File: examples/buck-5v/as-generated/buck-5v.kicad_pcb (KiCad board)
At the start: 2 copper layers, 126 x 56 mm, 11 parts, among them J1 12V IN, J2 5V OUT, U1 LM2596S-5

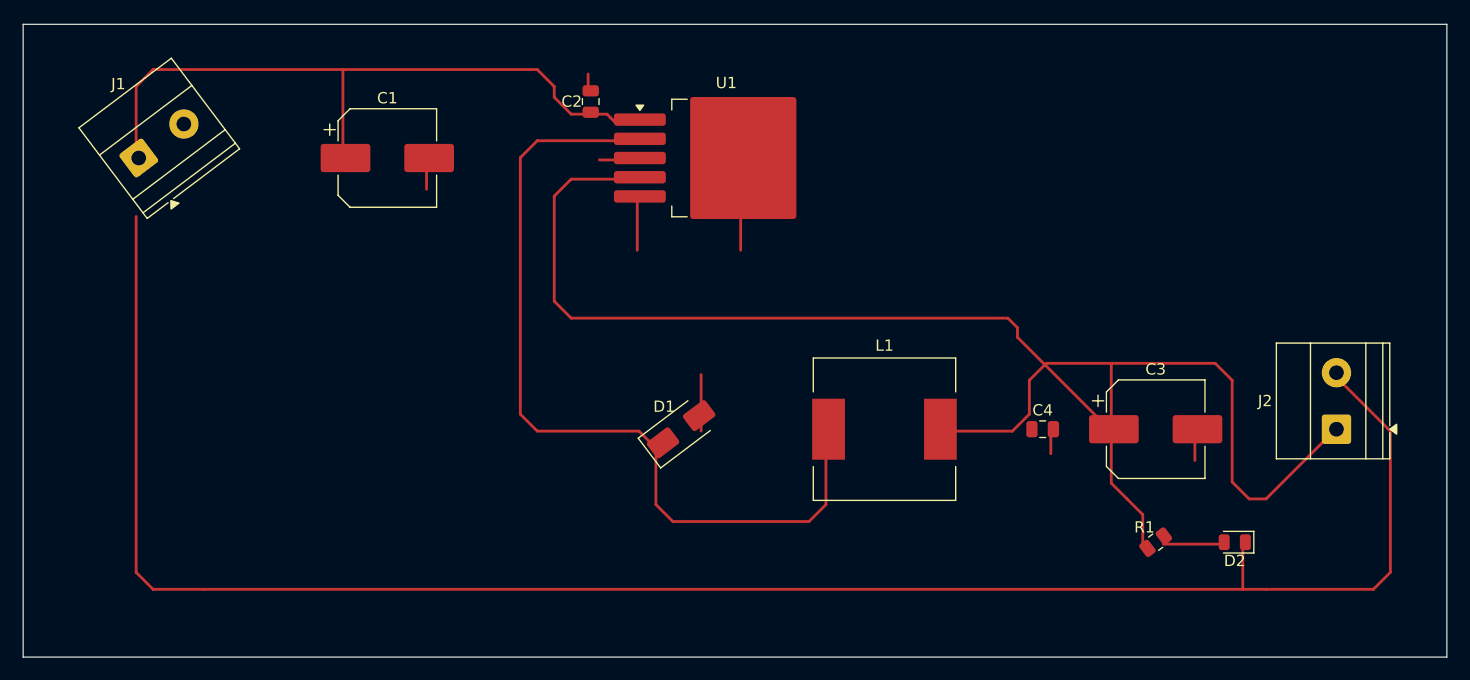
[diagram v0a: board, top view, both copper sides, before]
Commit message: Learn the drawing from the boards people drew
The brief for this round: relying on the autorouter and the numbers alone is
not enough - organise what pictorial correctness looks like from ordinary
circuits and open designs, and improve the drawing itself. So it starts in
KiCad's own demo corpus, measured and looked at, and ends with the habits
pushed into the generator.

tools/board_signature.py (new) reduces "looks autorouted" to five numbers.
Hand-routed two-layer boards cluster tightly: 10-47% of copper on the second
face, median segments 1.8-3.5 mm, 9-25 corners per decimetre, 91-98% of them
45s, 0.3-16 vias per decimetre. Rendering interf_u beside our boards says the
same thing in one glance: a layer has a direction, a bus travels as a bundle,
a person covers an offset with the long straight and one diagonal.

Three habits, now in the generator:

* Router.route(follow=...): cells beside a sibling net's path are discounted,
  so a bus (nets sharing a name prefix - I2S_*, SPI_*) travels as parallel
  lanes in one corridor. The discount is a fraction of a step, so it never
  buys a detour.
* _doglegged: every wiggly stretch is redrawn as the human stroke - the
  straight along the dominant direction plus one 45 - when the dogleg is
  clear, recursing into halves where a crossing blocks the whole. The op-amp
  board's median segment rose from 0.75 mm and its corner rate fell from
  38/dm; the FPGA board landed at 1.54 mm and 17.8/dm, inside the human band.
* Purposeful stitching: the 6 mm via carpet is gone. A ring at the rim, vias
  beside every back-layer crossing (where the plane is actually cut), and a
  coarse 12 mm mesh so no pour orphans. Vias/dm: buck 41 -> 18, carrier
  28 -> 13, all five inside the corpus band, pour_fragmented still silent.

Three failures the round produced and what they taught:

* pinned(): reshaping may not move copper off any point inside an own-net
  pad - the centre alone was not enough, a routed run touches off-centre and
  the ove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
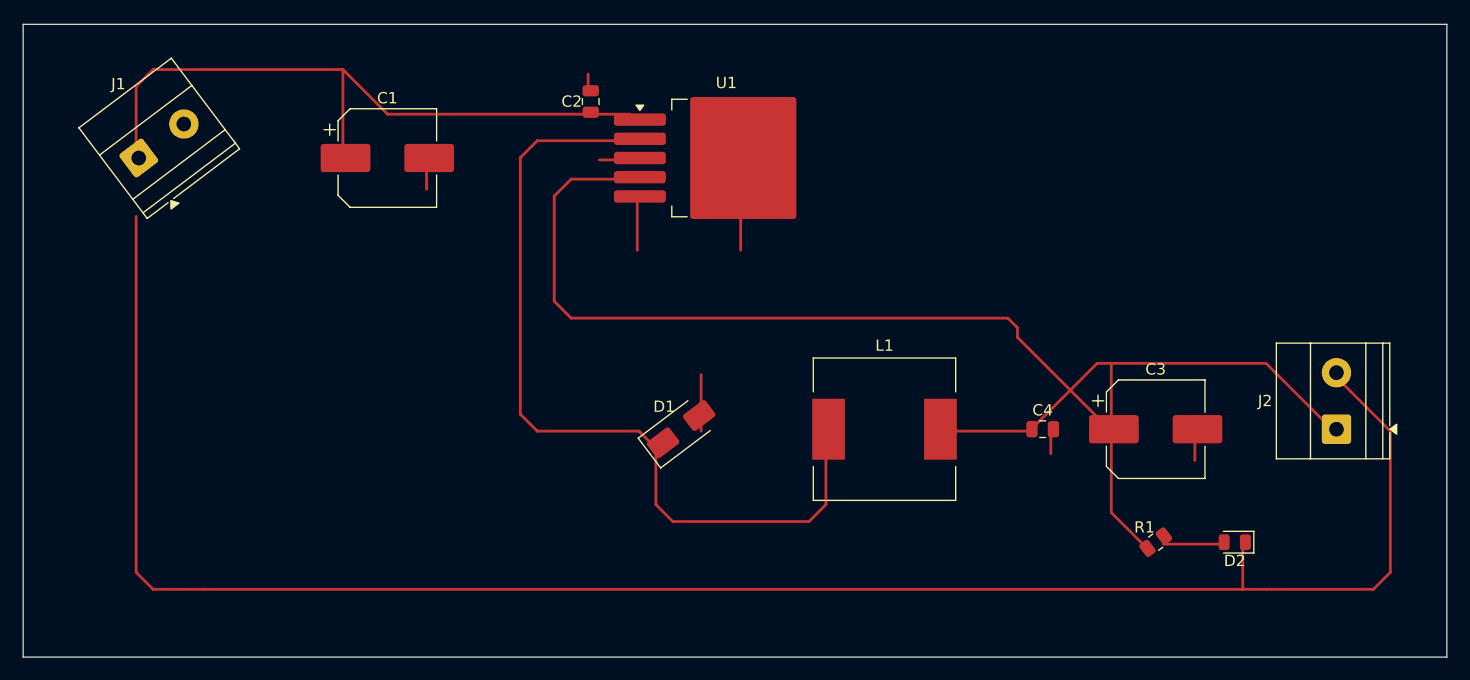
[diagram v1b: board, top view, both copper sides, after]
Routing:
- net /+5V: track 141.0 -> 129.0 mm
- net /+12V: track 61.9 -> 61.4 mm
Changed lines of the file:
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@@
 	(segment (start 111.5 64.0) (end 128.3 64.0) (width 0.25) (layer "F.Cu") (net 2))
 	(segment (start 128.3 64.0) (end 128.3 72.0) (width 0.25) (layer "F.Cu") (net 2))
-	(segment (start 128.3 64.0) (end 145.5 64.0) (width 0.25) (layer "F.Cu") (net 2))
-	(segment (start 145.5 64.0) (end 147.0 65.5) (width 0.25) (layer "F.Cu") (net 2))
-	(segment (start 147.0 65.5) (end 147.0 66.45) (width 0.25) (layer "F.Cu") (net 2))
-	(segment (start 147.0 66.45) (end 148.5 67.95) (width 0.25) (layer "F.Cu") (net 2))
-	(segment (start 148.5 67.95) (end 150.0 67.95) (width 0.25) (layer "F.Cu") (net 2))
-	(segment (start 150.0 67.95) (end 151.675 67.95) (width 0.25) (layer "F.Cu") (net 2))
-	(segment (start 151.675 67.95) (end 152.0 68.275) (width 0.25) (layer "F.Cu") (net 2))
-	(segment (start 152.0 68.275) (end 152.325 68.6) (width 0.25) (layer "F.Cu") (net 2))
-	(segment (start 152.325 68.6) (end 154.35 68.6) (width 0.25) (layer "F.Cu") (net 2))
+	(segment (start 128.3 64.0) (end 132.25 67.95) (width 0.25) (layer "F.Cu") (net 2))
+	(segment (start 132.25 67.95) (end 150.0 67.95) (width 0.25) (layer "F.Cu") (net 2))
+	(segment (start 150.0 67.95) (end 153.7 67.95) (width 0.25) (layer "F.Cu") (net 2))
+	(segment (start 153.7 67.95) (end 154.35 68.6) (width 0.25) (layer "F.Cu") (net 2))
 	(segment (start 154.35 70.3) (end 145.5 70.3) (width 0.25) (layer "F.Cu") (net 5))
 	(segment (start 145.5 70.3) (end 144.0 71.8) (width 0.25) (layer "F.Cu") (net 5))
@@
 	(segment (start 188.0 86.85) (end 188.0 87.7) (width 0.25) (layer "F.Cu") (net 3))
 	(segment (start 188.0 87.7) (end 196.3 96.0) (width 0.25) (layer "F.Cu") (net 3))
-	(segment (start 180.95 96.0) (end 187.55 96.0) (width 0.25) (layer "F.Cu") (net 3))
-	(segment (start 187.55 96.0) (end 189.05 94.5) (width 0.25) (layer "F.Cu") (net 3))
-	(segment (start 189.05 94.5) (end 189.05 91.5) (width 0.25) (layer "F.Cu") (net 3))
-	(segment (start 189.05 91.5) (end 190.55 90.0) (width 0.25) (layer "F.Cu") (net 3))
-	(segment (start 190.55 90.0) (end 196.3 90.0) (width 0.25) (layer "F.Cu") (net 3))
+	(segment (start 180.95 96.0) (end 189.05 96.0) (width 0.25) (layer "F.Cu") (net 3))
+	(segment (start 189.05 96.0) (end 195.05 90.0) (width 0.25) (layer "F.Cu") (net 3))
+	(segment (start 195.05 90.0) (end 196.3 90.0) (width 0.25) (layer "F.Cu") (net 3))
 	(segment (start 196.3 90.0) (end 196.3 96.0) (width 0.25) (layer "F.Cu") (net 3))
-	(segment (start 196.3 90.0) (end 205.5 90.0) (width 0.25) (layer "F.Cu") (net 3))
-	(segment (start 205.5 90.0) (end 207.0 91.5) (width 0.25) (layer "F.Cu") (net 3))
-	(segment (start 207.0 91.5) (end 207.0 100.5) (width 0.25) (layer "F.Cu") (net 3))
-	(segment (start 207.0 100.5) (end 208.5 102.0) (width 0.25) (layer "F.Cu") (net 3))
-	(segment (start 208.5 102.0) (end 210.0 102.0) (width 0.25) (layer "F.Cu") (net 3))
-	(segment (start 210.0 102.0) (end 216.0 96.0) (width 0.25) (layer "F.Cu") (net 3))
-	(segment (start 196.3 96.0) (end 196.3 100.606) (width 0.25) (layer "F.Cu") (net 3))
-	(segment (start 196.3 100.606) (end 197.694 102.0) (width 0.25) (layer "F.Cu") (net 3))
-	(segment (start 197.694 102.0) (end 199.088 103.394) (width 0.25) (layer "F.Cu") (net 3))
-	(segment (start 199.088 103.394) (end 199.0875 106.0) (width 0.25) (layer "F.Cu") (net 3))
+	(segment (start 196.3 90.0) (end 210.0 90.0) (width 0.25) (layer "F.Cu") (net 3))
+	(segment (start 210.0 90.0) (end 216.0 96.0) (width 0.25) (layer "F.Cu") (net 3))
+	(segment (start 196.3 96.0) (end 196.3 103.2125) (width 0.25) (layer "F.Cu") (net 3))
+	(segment (start 196.3 103.2125) (end 199.0875 106.0) (width 0.25) (layer "F.Cu") (net 3))
 	(segment (start 200.9125 106.0) (end 206.0625 106.0) (width 0.25) (layer "F.Cu") (net 4))
 	(segment (start 110.0 77.0) (end 110.0 108.5) (width 0.25) (layer "F.Cu") (net 1))

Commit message: A net may not cross its own copper
The reviewer looked at the plots, saw tracks driven through each other, and
asked whether the other checks were really passing. Both halves of the
answer were worth keeping. Measured directly - every pair of same-layer
segments on every reviewed board - there is not one crossing between
different nets: DRC reports zero errors, zero shorts, zero unconnected, and
it is not being fooled. What the plots show is a net crossing *itself*:
thirteen places on the FPGA board, one each on the op-amp and the buck.
Same potential, so DRC has nothing to say; no length ratio catches it; no
rule of ours looked. The checks were honest. The check list had a hole
exactly the shape of what the eye catches first.

route.self_crossing (new, warning, promoted by ai-generated) measures it:
two branches of one net crossing means the copper carries a redundant loop,
and a person never draws one. KiCad's demo corpus: 6 of 16 boards carry one
to three, at dense escapes.

_unlooped (new pass) is the fix, as a graph question: split every same-net
crossing so the X is a node, and while any cycle remains in the net's
copper, remove the longest junction-to-junction chain of the cycle -
connectivity is kept by definition, a cycle has two ways round, and the
amputated X becomes an ordinary corner. The clearance oracle now also
refuses to let _doglegged or _straighten draw a new X over their own net.

The cutter was wrong twice before it was right, both times the same lesson:
KiCad's connectivity is geometric, a track graph is endpoint topology, and
the difference is exactly a pad. The escape fan draws a micro-hook inside
an off-grid pad - the overlap is the connection - and the graph read it as
a dangling loop and amputated the pad's only feed. Nodes inside an own-net
pad are anchors now, a cycle wholly inside one pad is immune, and segments
passing over a pad are split so the feed is a node the cut must respect.

Self-crossings on the five reviewed boards: 0/0/0/0/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
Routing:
- net /SW: track 74.7 -> 62.2 mm
- net /+5V: track 129.0 -> 123.3 mm
- net /+12V: track 61.4 -> 57.7 mm
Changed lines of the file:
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@@
 	(gr_line (start 226.0 116.0) (end 100.0 116.0) (stroke (width 0.1) (type default)) (layer "Edge.Cuts"))
 	(gr_line (start 100.0 116.0) (end 100.0 60.0) (stroke (width 0.1) (type default)) (layer "Edge.Cuts"))
-	(segment (start 110.0 72.0) (end 110.0 65.5) (width 0.25) (layer "F.Cu") (net 2))
-	(segment (start 110.0 65.5) (end 111.5 64.0) (width 0.25) (layer "F.Cu") (net 2))
-	(segment (start 111.5 64.0) (end 128.3 64.0) (width 0.25) (layer "F.Cu") (net 2))
-	(segment (start 128.3 64.0) (end 128.3 72.0) (width 0.25) (layer "F.Cu") (net 2))
-	(segment (start 128.3 64.0) (end 132.25 67.95) (width 0.25) (layer "F.Cu") (net 2))
-	(segment (start 132.25 67.95) (end 150.0 67.95) (width 0.25) (layer "F.Cu") (net 2))
-	(segment (start 150.0 67.95) (end 153.7 67.95) (width 0.25) (layer "F.Cu") (net 2))
-	(segment (start 153.7 67.95) (end 154.35 68.6) (width 0.25) (layer "F.Cu") (net 2))
-	(segment (start 154.35 70.3) (end 145.5 70.3) (width 0.25) (layer "F.Cu") (net 5))
-	(segment (start 145.5 70.3) (end 144.0 71.8) (width 0.25) (layer "F.Cu") (net 5))
-	(segment (start 144.0 71.8) (end 144.0 94.5) (width 0.25) (layer "F.Cu") (net 5))
-	(segment (start 144.0 94.5) (end 145.5 96.0) (width 0.25) (layer "F.Cu") (net 5))
-	(segment (start 145.5 96.0) (end 154.5 96.0) (width 0.25) (layer "F.Cu") (net 5))
-	(segment (start 154.5 96.0) (end 156.0 97.5) (width 0.25) (layer "F.Cu") (net 5))
-	(segment (start 156.0 97.5) (end 156.0 102.5) (width 0.25) (layer "F.Cu") (net 5))
-	(segment (start 156.0 102.5) (end 157.5 104.0) (width 0.25) (layer "F.Cu") (net 5))
-	(segment (start 157.5 104.0) (end 169.55 104.0) (width 0.25) (layer "F.Cu") (net 5))
-	(segment (start 169.55 104.0) (end 171.05 102.5) (width 0.25) (layer "F.Cu") (net 5))
-	(segment (start 171.05 102.5) (end 171.05 96.0) (width 0.25) (layer "F.Cu") (net 5))
-	(segment (start 154.35 73.7) (end 148.5 73.7) (width 0.25) (layer "F.Cu") (net 3))
-	(segment (start 148.5 73.7) (end 147.0 75.2) (width 0.25) (layer "F.Cu") (net 3))
-	(segment (start 147.0 75.2) (end 147.0 84.5) (width 0.25) (layer "F.Cu") (net 3))
-	(segment (start 147.0 84.5) (end 148.5 86.0) (width 0.25) (layer "F.Cu") (net 3))
-	(segment (start 148.5 86.0) (end 187.15 86.0) (width 0.25) (layer "F.Cu") (net 3))
-	(segment (start 187.15 86.0) (end 188.0 86.85) (width 0.25) (layer "F.Cu") (net 3))
-	(segment (start 188.0 86.85) (end 188.0 87.7) (width 0.25) (layer "F.Cu") (net 3))
-	(segment (start 188.0 87.7) (end 196.3 96.0) (width 0.25) (layer "F.Cu") (net 3))
-	(segment (start 180.95 96.0) (end 189.05 96.0) (width 0.25) (layer "F.Cu") (net 3))
-	(segment (start 189.05 96.0) (end 195.05 90.0) (width 0.25) (layer "F.Cu") (net 3))
-	(segment (start 195.05 90.0) (end 196.3 90.0) (width 0.25) (layer "F.Cu") (net 3))
-	(segment (start 196.3 90.0) (end 196.3 96.0) (width 0.25) (layer "F.Cu") (net 3))
-	(segment (start 196.3 90.0) (end 210.0 90.0) (width 0.25) (layer "F.Cu") (net 3))
-	(segment (start 210.0 90.0) (end 216.0 96.0) (width 0.25) (layer "F.Cu") (net 3))
-	(segment (start 196.3 96.0) (end 196.3 103.2125) (width 0.25) (layer "F.Cu") (net 3))
-	(segment (start 196.3 103.2125) (end 199.0875 106.0) (width 0.25) (layer "F.Cu") (net 3))
-	(segment (start 200.9125 106.0) (end 206.0625 106.0) (width 0.25) (layer "F.Cu") (net 4))
 	(segment (start 110.0 77.0) (end 110.0 108.5) (width 0.25) (layer "F.Cu") (net 1))
 	(segment (start 110.0 108.5) (end 111.5 110.0) (width 0.25) (layer "F.Cu") (net 1))
@@
 	(segment (start 203.7 96.0) (end 203.7 98.6) (width 0.25) (layer "F.Cu") (net 1))
 	(segment (start 207.9375 106.0) (end 207.938 110.0) (width 0.25) (layer "F.Cu") (net 1))
+	(segment (start 110.0 72.0) (end 110.0 71.83) (width 0.25) (layer "F.Cu") (net 2))
+	(segment (start 110.0 71.83) (end 120.47 71.83) (width 0.25) (layer "F.Cu") (net 2))
+	(segment (start 120.47 71.83) (end 128.3 64.0) (width 0.25) (layer "F.Cu") (net 2))
+	(segment (start 128.3 64.0) (end 128.3 71.83) (width 0.25) (layer "F.Cu") (net 2))
+	(segment (start 128.3 71.83) (end 128.3 72.0) (width 0.25) (layer "F.Cu") (net 2))
+	(segment (start 128.3 64.0) (end 132.25 67.95) (width 0.25) (layer "F.Cu") (net 2))
+	(segment (start 132.25 67.95) (end 150.0 67.95) (width 0.25) (layer "F.Cu") (net 2))
+	(segment (start 150.0 67.95) (end 150.23 67.95) (width 0.25) (layer "F.Cu") (net 2))
+	(segment (start 150.23 67.95) (end 153.7 67.95) (width 0.25) (layer "F.Cu") (net 2))
+	(segment (start 153.7 67.95) (end 154.35 68.6) (width 0.25) (layer "F.Cu") (net 2))
+	(segment (start 154.35 70.3) (end 145.5 70.3) (width 0.25) (layer "F.Cu") (net 5))
+	(segment (start 145.5 70.3) (end 144.0 71.8) (width 0.25) (layer "F.Cu") (net 5))
+	(segment (start 144.0 71.8) (end 144.0 94.5) (width 0.25) (layer "F.Cu") (net 5))
+	(segment (start 144.0 94.5) (end 145.5 96.0) (width 0.25) (layer "F.Cu") (net 5))
+	(segment (start 145.5 96.0) (end 155.483 96.0) (width 0.25) (layer "F.Cu") (net 5))
+	(segment (start 155.483 96.0) (end 156.0 96.517) (width 0.25) (layer "F.Cu") (net 5))
+	(segment (start 156.0 96.517) (end 156.517 97.034) (width 0.25) (layer "F.Cu") (net 5))
+	(segment (start 156.517 97.034) (end 170.0164 97.0336) (width 0.25) (layer "F.Cu") (net 5))
+	(segment (start 170.0164 97.0336) (end 171.05 96.0) (width 0.25) (layer "F.Cu") (net 5))
+	(segment (start 154.35 73.7) (end 148.5 73.7) (width 0.25) (layer "F.Cu") (net 3))
+	(segment (start 148.5 73.7) (end 147.0 75.2) (width 0.25) (layer "F.Cu") (net 3))
+	(segment (start 147.0 75.2) (end 147.0 84.5) (width 0.25) (layer "F.Cu") (net 3))
+	(segment (start 147.0 84.5) (end 148.5 86.0) (width 0.25) (layer "F.Cu") (net 3))
+	(segment (start 148.5 86.0) (end 187.15 86.0) (width 0.25) (layer "F.Cu") (net 3))
+	(segment (start 187.15 86.0) (end 188.0 86.85) (width 0.25) (layer "F.Cu") (net 3))
+	(segment (start 188.0 86.85) (end 188.0 87.7) (width 0.25) (layer "F.Cu") (net 3))
+	(segment (start 188.0 87.7) (end 190.3 90.0) (width 0.25) (layer "F.Cu") (net 3))
+	(segment (start 180.95 96.0) (end 181.18 96.0) (width 0.25) (layer "F.Cu") (net 3))
+	(segment (start 181.18 96.0) (end 189.05 96.0) (width 0.25) (layer "F.Cu") (net 3))
+	(segment (start 189.05 96.0) (end 189.05 95.83) (width 0.25) (layer "F.Cu") (net 3))
+	(segment (start 189.05 95.83) (end 189.05 91.25) (width 0.25) (layer "F.Cu") (net 3))
+	(segment (start 189.05 91.25) (end 190.3 90.0) (width 0.25) (layer "F.Cu") (net 3))
+	(segment (start 190.3 90.0) (end 196.3 90.0) (width 0.25) (layer "F.Cu") (net 3))
+	(segment (start 196.3 90.0) (end 196.3 95.83) (width 0.25) (layer "F.Cu") (net 3))
+	(segment (start 196.3 95.83) (end 196.3 96.0) (width 0.25) (layer "F.Cu") (net 3))
+	(segment (start 196.3 96.0) (end 196.3 103.2125) (width 0.25) (layer "F.Cu") (net 3))
+	(segment (start 196.3 103.2125) (end 199.0875 106.0) (width 0.25) (layer "F.Cu") (net 3))
+	(segment (start 196.3 90.0) (end 210.0 90.0) (width 0.25) (layer "F.Cu") (net 3))
+	(segment (start 210.0 90.0) (end 216.0 96.0) (width 0.25) (layer "F.Cu") (net 3))
+	(segment (start 200.9125 106.0) (end 206.0625 106.0) (width 0.25) (layer "F.Cu") (net 4))
 )
